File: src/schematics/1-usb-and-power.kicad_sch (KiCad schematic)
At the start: 51 parts, among them Q101 NX6008NBKW, U101 MP5016HGQH, U102 BQ24392RSER, U103 FUSB302BMPX, U104 TPS628512DRLR

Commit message: Added part numbers for the capacitors.
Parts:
- C103, C104, C107, C111: Manufacturer (none) -> Samsung; Manufacturer2 (none) -> Samsung; Manufacturer2PartNumber (none) -> CL05A104KA5NNNC; ManufacturerPartNumber (none) -> CL05B104KA5NNNC
- C106: Manufacturer (none) -> Yageo; Manufacturer2 (none) -> Walsin; Manufacturer2PartNumber (none) -> 0402N390J500CT; ManufacturerPartNumber (none) -> CC0402JRNPO9BN390
- C108: Manufacturer (none) -> Cal-Chip; Manufacturer2 (none) -> Yageo; Manufacturer2PartNumber (none) -> CC0402JRNPO9BN101; ManufacturerPartNumber (none) -> GMC04CG101G50NT
- C109, C110, C112, C113, C118, C119, C120, C121: ManufacturerPartNumber (none) -> CL05A475MP5NRNC
- C114, C115: Manufacturer (none) -> Murata; Manufacturer2 (none) -> Murata; Manufacturer2PartNumber (none) -> GRT1555C1H471FA02D; ManufacturerPartNumber (none) -> GCM1555C1H471FA16D
- C122: Manufacturer (none) -> Vishay; Manufacturer2 (none) -> TDK; Manufacturer2PartNumber (none) -> CGA2B3X7R1H473K050BB; ManufacturerPartNumber (none) -> VJ0402Y473KXQCW1BC
- FB101: Package (none) -> WLBD2012

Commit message: Added part numbers for the resistors.
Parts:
- R101: Manufacturer (none) -> Yageo; Manufacturer2 (none) -> Yageo; Manufacturer2PartNumber (none) -> AC0402FR-07300KL; ManufacturerPartNumber (none) -> RC0402FR-07300KL
- R102: Manufacturer (none) -> Yageo; Manufacturer2 (none) -> Walsin; Manufacturer2PartNumber (none) -> WR04X000PTL; ManufacturerPartNumber (none) -> RC0402FR-070RL
- R103: Manufacturer (none) -> Walsin; Manufacturer2 (none) -> Yageo; Manufacturer2PartNumber (none) -> RC0402FR-071KL; ManufacturerPartNumber (none) -> WR04X1001FTL
- R104, R105, R106, R110, R111: Manufacturer (none) -> Walsin; Manufacturer2 (none) -> Yageo; Manufacturer2PartNumber (none) -> RC0402FR-0733KL; ManufacturerPartNumber (none) -> WR04X3302FTL
- R107, R108: Manufacturer (none) -> Vishay; Manufacturer2 (none) -> Vishay; Manufacturer2PartNumber (none) -> CRCW04022R20FKEDC; ManufacturerPartNumber (none) -> RMCF0402FT2R20
- R109, R114: Manufacturer (none) -> Walsin; Manufacturer2 (none) -> Yageo; Manufacturer2PartNumber (none) -> RC0402FR-073K3L; ManufacturerPartNumber (none) -> CRCW04022R20FKED
- R112: Manufacturer (none) -> Walsin; Manufacturer2 (none) -> Yageo; Manufacturer2PartNumber (none) -> RC0402FR-0788K7L; ManufacturerPartNumber (none) -> WR04X8872FTL
- R113: Manufacturer (none) -> Walsin; Manufacturer2 (none) -> Yageo; Manufacturer2PartNumber (none) -> RC0402FR-0719K6L; ManufacturerPartNumber (none) -> WR04X1962FTL

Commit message: Clean up the remaining ERC flags.
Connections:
- net GND renamed GND_PWRIN
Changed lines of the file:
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@@
     )
     (pin "1")
-    (pin "2")
+    (pin "2" (alternate "P2_PWROUT"))
     (instances
       (project "msf-owl-clock"
@@
       (effects (font (size 1.27 1.27)) hide)
     )
-    (pin "1")
-    (pin "2")
-    (instances
-      (project "msf-owl-clock"
+    (pin "1" (alternate "P1_PWRIN"))
+    (pin "2" (alternate "P2_PWROUT"))
+    (instances
+      (project "msf-owl-clock"

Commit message: Some footprint / net bugfixes identified whilst generating the initial PCB.
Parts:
- D101: footprint restall-generic-sot:SOD-323 -> restall-generic-sot:SOD323
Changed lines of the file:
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@@
       (effects (font (size 1.27 1.27)) (justify left))
     )
-    (property "Footprint" "restall-generic-sot:SOD-323" (at 91.44 214.884 0)
+    (property "Footprint" "restall-generic-sot:SOD323" (at 91.44 214.884 0)
       (effects (font (size 1.27 1.27)) (justify right) hide)
     )

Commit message: Started to lay out the PCB.
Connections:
- net D_{+} renamed D+
- net D+: no longer U102.3 (DP_HOST)
- net D_{-} renamed D-
- net D-: no longer U102.2 (DM_HOST)
- net GND_PWRIN renamed GND
- new net MCU.D+: U102.3 (DP_HOST)
- new net MCU.D-: U102.2 (DM_HOST)
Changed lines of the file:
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@@
     (company "Pete Restall <pete@restall.net>")
   )
-  (bus_alias "USB_DATA" (members "D_{+}" "D_{-}"))
+  (bus_alias "USB_DATA" (members "D+" "D-"))
   (junction (at 48.26 63.5) (diameter 0) (color 0 0 0 0)
   )
@@
     (effects (font (size 1.27 1.27)) (justify right bottom))
   )
-  (label "D_{+}" (at 243.84 124.46 0) (fields_autoplaced)
+  (label "D+" (at 243.84 124.46 0) (fields_autoplaced)
     (effects (font (size 1.27 1.27)) (justify left bottom))
   )
@@
     (effects (font (size 1.27 1.27)) (justify right bottom))
   )
-  (label "D_{+}" (at 378.46 125.73 180) (fields_autoplaced)
+  (label "MCU.D+" (at 378.46 125.73 180) (fields_autoplaced)
     (effects (font (size 1.27 1.27)) (justify right bottom))
   )
@@
     (effects (font (size 1.27 1.27)) (justify left bottom))
   )
-  (label "D_{-}" (at 378.46 128.27 180) (fields_autoplaced)
+  (label "MCU.D-" (at 378.46 128.27 180) (fields_autoplaced)
     (effects (font (size 1.27 1.27)) (justify right bottom))
   )
@@
     (effects (font (size 1.27 1.27)) (justify right bottom))
   )
-  (label "D_{-}" (at 243.84 129.54 0) (fields_autoplaced)
+  (label "D-" (at 243.84 129.54 0) (fields_autoplaced)
     (effects (font (size 1.27 1.27)) (justify left bottom))
   )
@@
     (effects (font (size 1.27 1.27)) (justify left))
   )
-  (hierarchical_label "{USB_DATA}" (shape bidirectional) (at 386.08 91.44 0) (fields_autoplaced)
+  (hierarchical_label "MCU{USB_DATA}" (shape bidirectional) (at 386.08 91.44 0) (fields_autoplaced)
     (effects (font (size 1.27 1.27)) (justify left))
   )

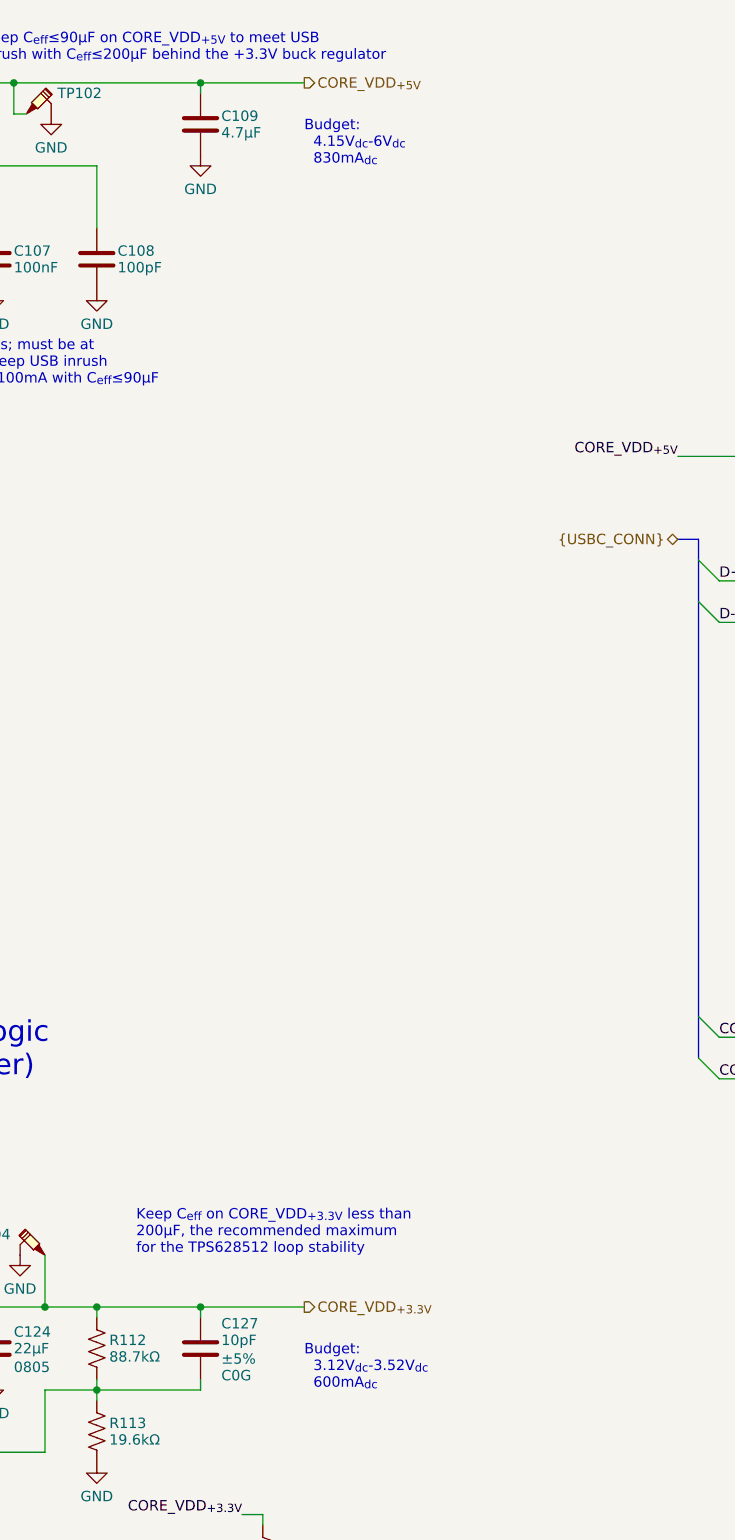
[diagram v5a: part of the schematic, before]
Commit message: Updated to allow up to 1.44W for the SD card, which is actually what UHS-I specifications are measured at; 0.72W is the limit for the default speed mode / driver strength.
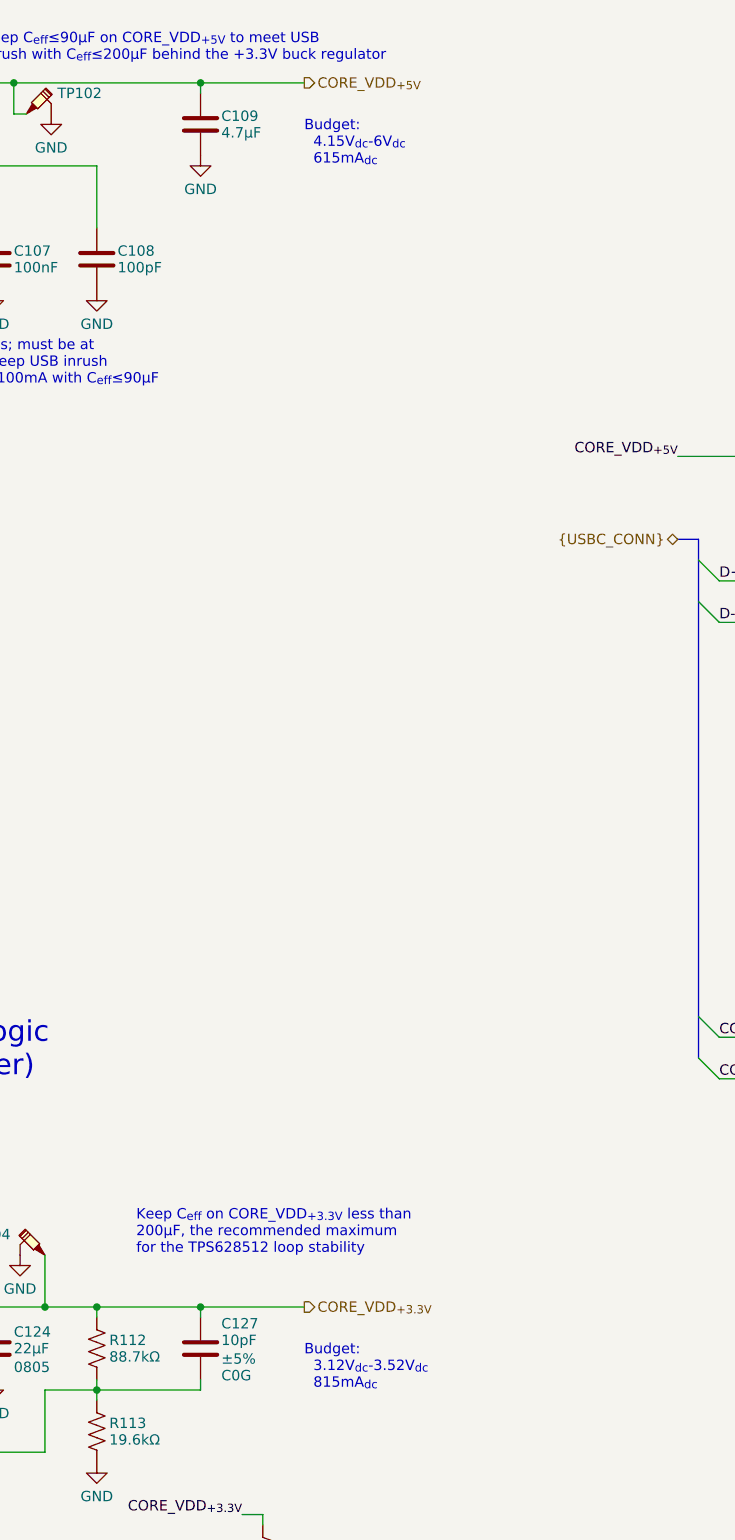
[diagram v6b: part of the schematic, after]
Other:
- note added: "Budget: 3.12V_{dc}-3.52V_{dc} 815mA_{dc}"
- note added: "Budget: 4.15V_{dc}-6V_{dc} 615mA_{dc}"
- note removed: "Budget: 3.12V_{dc}-3.52V_{dc} 600mA_{dc}"
- note removed: "Budget: 4.15V_{dc}-6V_{dc} 830mA_{dc}"
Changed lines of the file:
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@@
     (effects (font (size 1.27 1.27)) (justify left bottom))
   )
-  (text "Budget:\n  4.15V_{dc}-6V_{dc}\n  830mA_{dc}" (at 193.04 73.66 0)
+  (text "Budget:\n  4.15V_{dc}-6V_{dc}\n  615mA_{dc}" (at 193.04 73.66 0)
     (effects (font (size 1.27 1.27)) (justify left bottom))
   )
@@
     (effects (font (size 1.27 1.27)) (justify left bottom))
   )
-  (text "Budget:\n  3.12V_{dc}-3.52V_{dc}\n  600mA_{dc}" (at 193.04 223.52 0)
+  (text "Budget:\n  3.12V_{dc}-3.52V_{dc}\n  815mA_{dc}" (at 193.04 223.52 0)
     (effects (font (size 1.27 1.27)) (justify left bottom))
   )

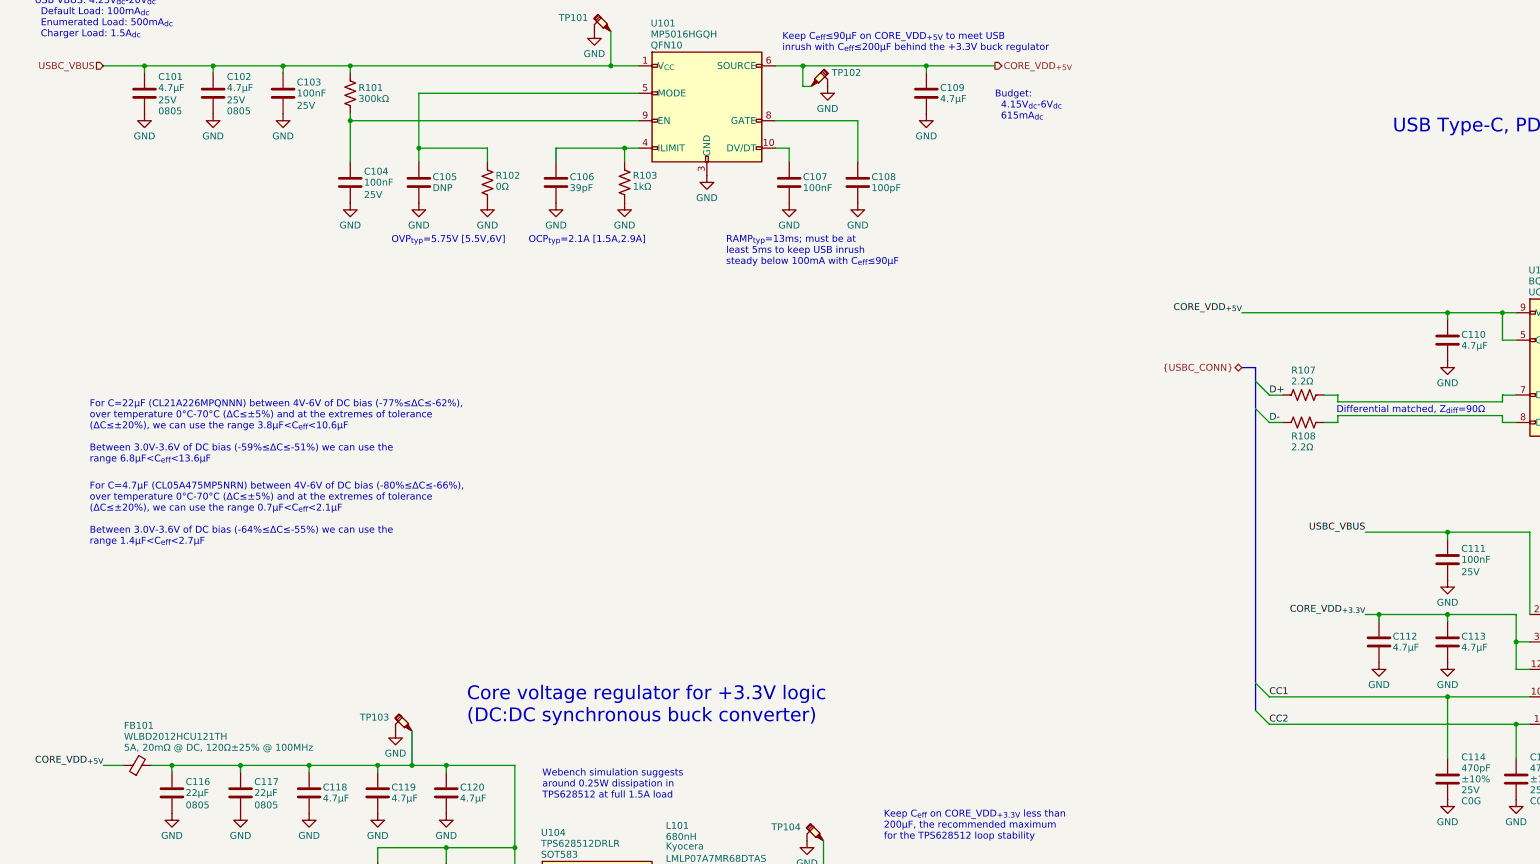
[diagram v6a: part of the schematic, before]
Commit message: PCB routing.  Fixed most of the DRC violations.
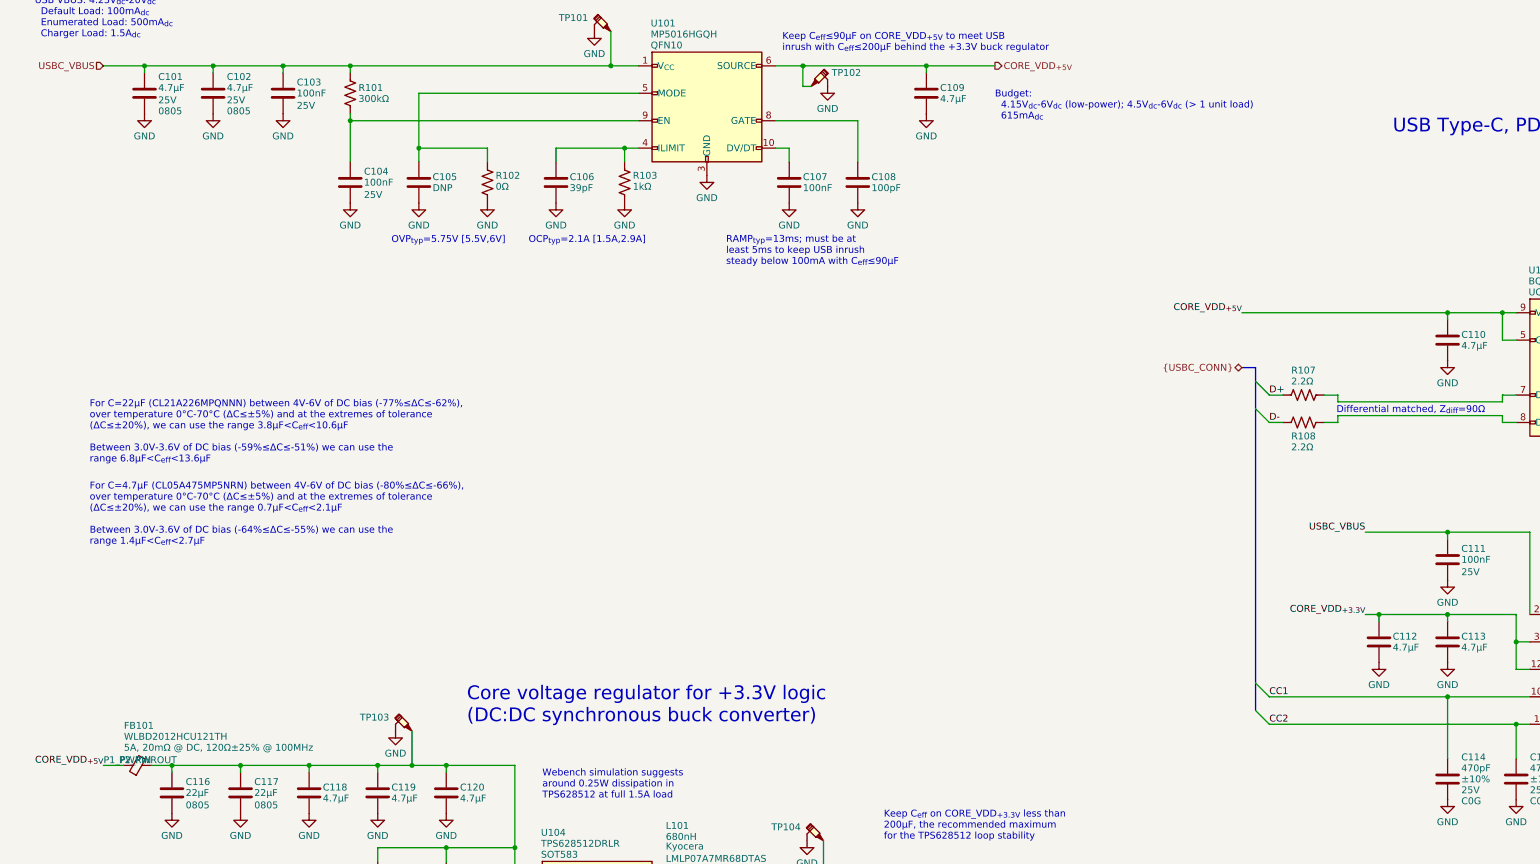
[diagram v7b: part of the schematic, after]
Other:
- note added: "Budget: 4.15V_{dc}-6V_{dc} (low-power); 4.5V_{dc}-6V_{dc} (> 1 unit load) 615mA_{dc}"
- note removed: "Budget: 4.15V_{dc}-6V_{dc} 615mA_{dc}"
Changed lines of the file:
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@@
     (effects (font (size 1.27 1.27)) (justify left bottom))
   )
-  (text "Budget:\n  4.15V_{dc}-6V_{dc}\n  615mA_{dc}" (at 193.04 73.66 0)
+  (text "Budget:\n  4.15V_{dc}-6V_{dc} (low-power); 4.5V_{dc}-6V_{dc} (> 1 unit load)\n  615mA_{dc}"
+    (at 193.04 73.66 0)
     (effects (font (size 1.27 1.27)) (justify left bottom))
   )

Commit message: Further tweaks, tidy-ups and silkscreen labelling.
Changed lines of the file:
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@@
   (title_block
     (title "MSF Owl Clock - USB and Core Power Module")
+    (date "June 2024")
     (rev "0.1")
     (company "Pete Restall <pete@restall.net>")
